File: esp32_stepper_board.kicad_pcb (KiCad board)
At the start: 2 copper layers, 99.9 x 70.2 mm, 30 parts, among them J1 Aux2_GPIO, J10 Aux1_I2C, J11 IO0_IO2_JP, J2 DC_PWR, J3 Servo, J4 Stepper A/X, J5 Stepper B/Y, J6 Stepper C/Y, J7 Endstop A/X, J8 Endstop B/Y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

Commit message: fix silk screen label for c/z stepper
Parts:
- J6: value Stepper C/Y -> Stepper C/Z
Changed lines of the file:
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@@
     (links 122)
     (no_connects 0)
-    (area 40.818999 32.436999 140.918001 102.818001)
+    (area 100.762999 63.271138 200.862001 135.530001)
     (thickness 1.6)
     (drawings 6)
@@
       (effects (font (size 1 1) (thickness 0.15)))
     )
-    (fp_text value "Stepper C/Y" (at 2.921 -3.048 180) (layer F.SilkS)
-      (effects (font (size 1 1) (thickness 0.15)))
-    )
+    (fp_text value "Stepper C/Z" (at 2.921 -3.048 180) (layer F.SilkS)
+      (effects (font (size 1 1) (thickness 0.15)))
+    )

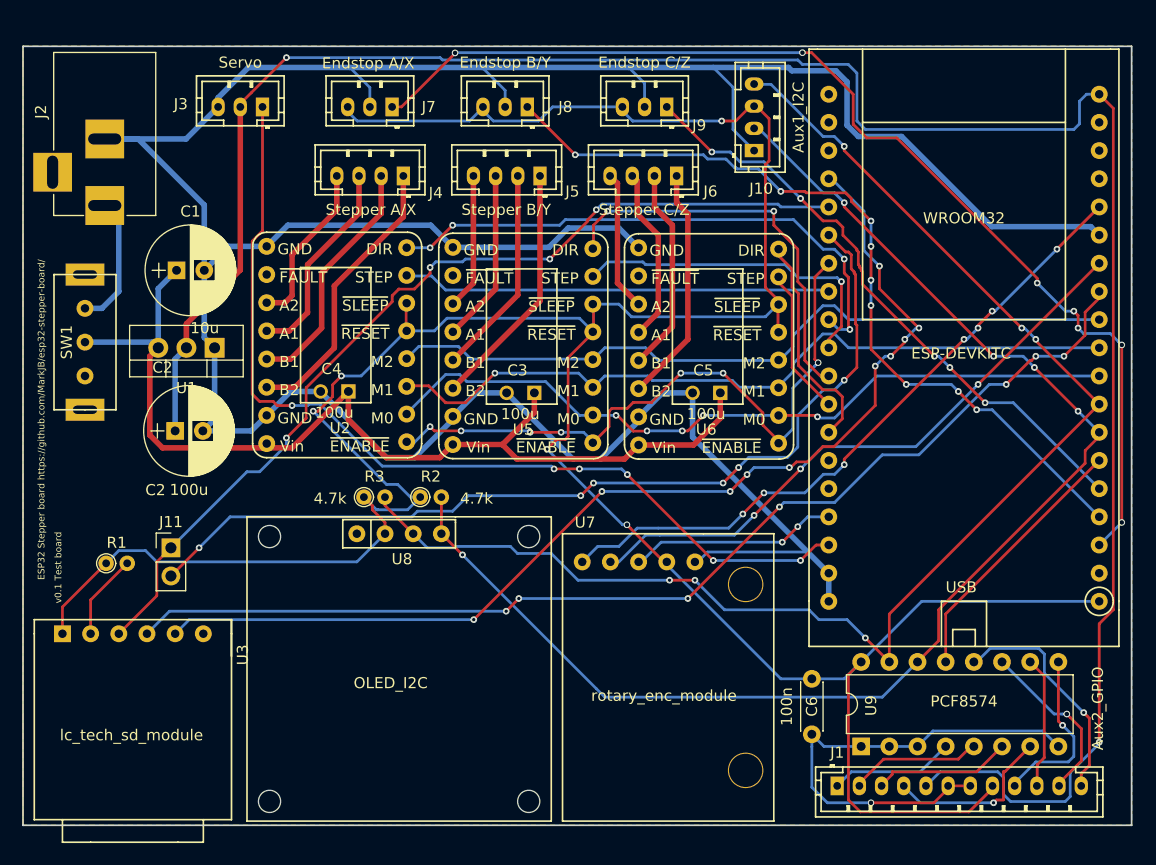
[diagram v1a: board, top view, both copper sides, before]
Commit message: Fixed devkit footprint and rerouted board
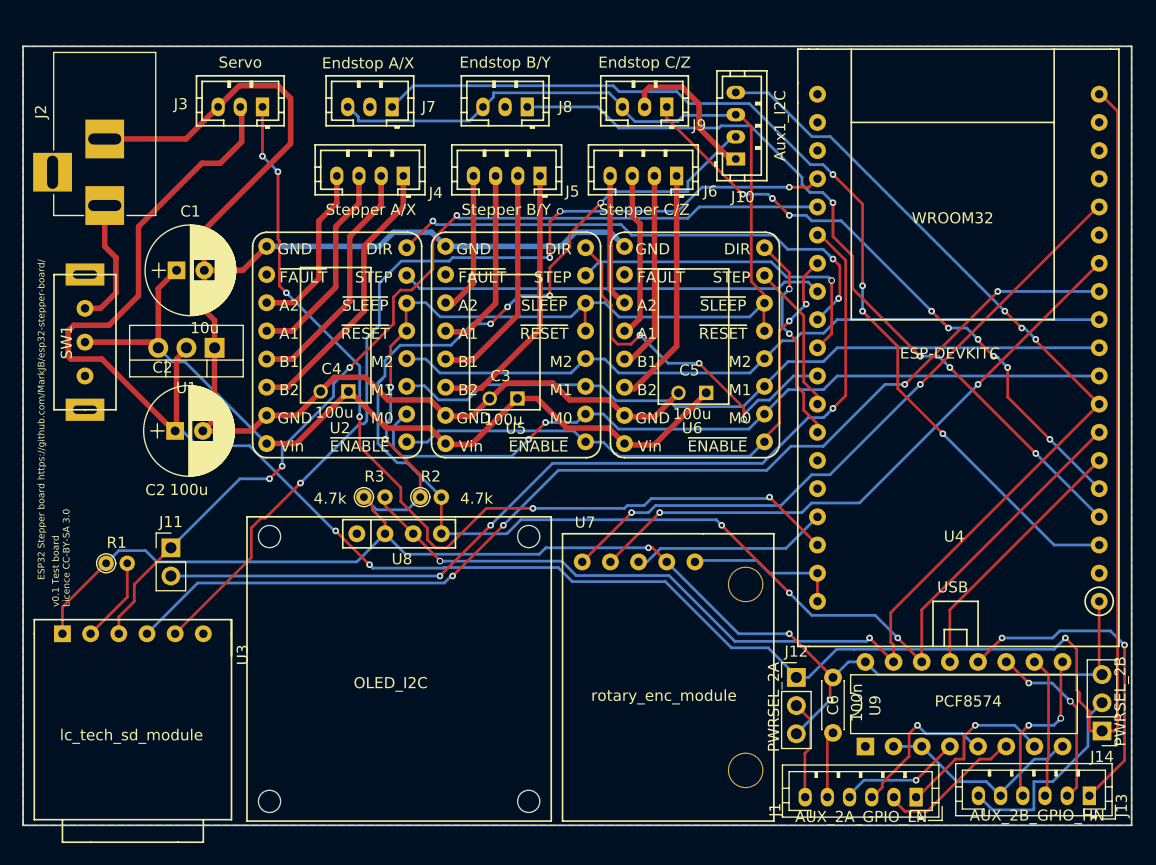
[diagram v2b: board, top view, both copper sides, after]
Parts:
- added J12: PWRSEL_2A, Pin_Headers:Pin_Header_Straight_1x03_Pitch2.54mm, F.Cu at (170.6, 120.4)
- added J13: AUX_2B_GPIO_HN, Connectors_JST:JST_PH_B6B-PH-K_06x2.00mm_Straight, F.Cu at (197.0, 131.1)
- added J14: PWRSEL_2B, Pin_Headers:Pin_Header_Straight_1x03_Pitch2.54mm, F.Cu at (198.1, 125.2)
- J1: value Aux2_GPIO -> AUX_2A_GPIO_LN; footprint Connectors_JST:JST_PH_B12B-PH-K_12x2.00mm_Straight -> Connectors_JST:JST_PH_B6B-PH-K_06x2.00mm_Straight
- moved J1 7.18 mm to (181.4, 131.2), turned to 180 degrees
- moved C6 1.91 mm to (173.9, 120.4)
- moved J10 1.82 mm to (165.1, 73.7)
- moved C3 1.61 mm to (145.4, 95.2)
- moved U6 1.28 mm to (161.9, 89.2)
- moved C5 1.27 mm to (162.4, 94.7)
- moved U5 0.66 mm to (145.8, 89.2)
- moved U9 0.38 mm to (176.8, 126.6)
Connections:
- J1 pad 1: /GPIO_EX0 -> /GPIO_EX3
- J1 pad 2: /GPIO_EX1 -> /GPIO_EX2
- J1 pad 3: /GPIO_EX2 -> /GPIO_EX1
- J1 pad 4: /GPIO_EX3 -> /GPIO_EX0
- J1 pad 5: /5v -> /GND
- J1 pad 6: /GND -> /PWR1
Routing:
- net /GND: track 336.7 -> 197.0 mm, vias 1 -> 0
- net /3v3: track 275.2 -> 246.7 mm
- net /PWR2: track 0.00 -> 18.7 mm
- net /SDA1: track 123.9 -> 138.5 mm, vias 5 -> 7
- net /12v: track 91.3 -> 76.7 mm
- net /5v: track 200.4 -> 213.5 mm, vias 2 -> 3
- net /SD_MISO: track 97.7 -> 85.0 mm, vias 10 -> 4
- net /~ES_A/X: track 100.1 -> 89.6 mm, vias 7 -> 4
- net /PWR1: track 0.00 -> 9.02 mm
- net /GPIO_EX7: track 20.9 -> 29.8 mm, vias 1 -> 2
- net /~STEP_EN: track 60.2 -> 52.8 mm, vias 7 -> 2
- net /A/X_DIR: track 50.9 -> 47.5 mm, vias 4 -> 3
- net /STEP_M0: track 68.6 -> 71.8 mm, vias 5 -> 2
- net /~ES_B/Y: track 73.8 -> 70.9 mm, vias 9 -> 4
- net /GPIO_EX1: track 11.9 -> 14.5 mm, vias 0 -> 1
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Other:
- board text added: "v0.1 Test board Licence CC-BY-SA 3.0"
- board text removed: "v0.1 Test board"

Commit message: fix flat cap silk and various silk issue
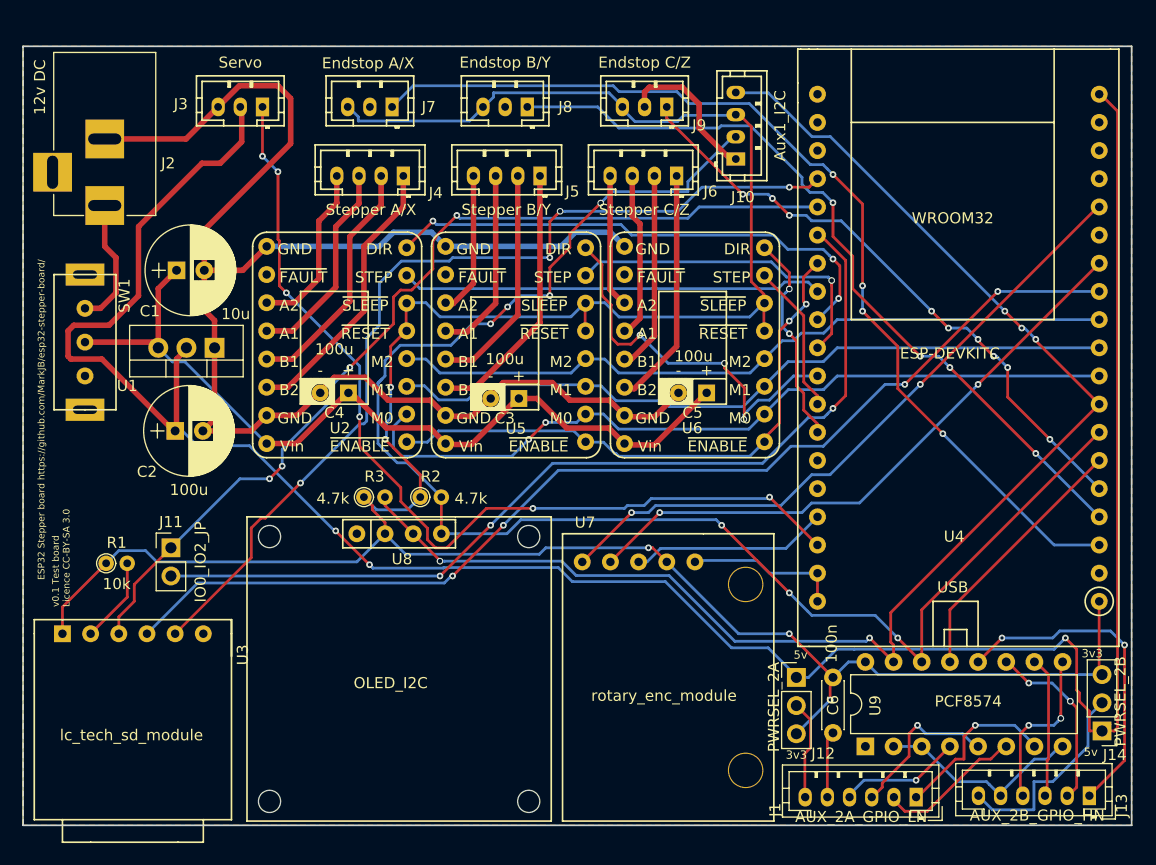
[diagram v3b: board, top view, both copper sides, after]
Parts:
- C3, C4, C5: footprint custom:C_Radial_lying_flat_D8_L11_P2.5 -> custom:Cap_laying_flat_2.5mm_lead_pitch
- moved C4 2.73 mm to (128.9, 97.0)
- moved C5 2.60 mm to (161.2, 97.0)
- moved C3 2.56 mm to (144.3, 97.5)
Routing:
- net /B/Y_DIR: track 33.9 -> 35.3 mm
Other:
- board text added: "12v DC"
- board text added: "3v3"
- board text added: "5v"

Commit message: Fixed devkitc footprint silk, rotated devkitc footprint, fix stepper pwr track width, c_step pin on IO23 (moved from gnd), moved renc_sw from tx.
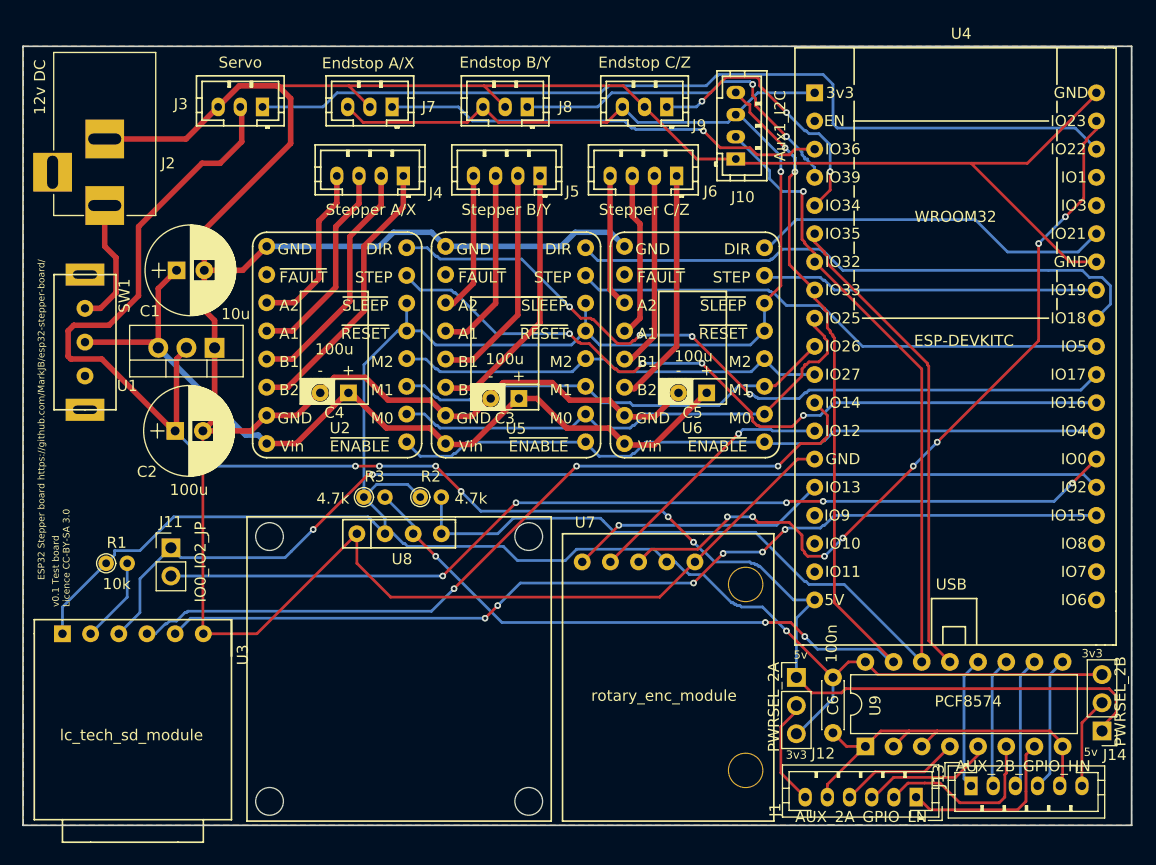
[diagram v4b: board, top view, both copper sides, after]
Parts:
- moved U4 52.5 mm to (172.2, 67.7), turned to 0 degrees
- moved J13 10.7 mm to (186.3, 130.2), turned to 0 degrees
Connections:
- U4 pad 32: /C/Z_DIR -> /GND
- U4 pad 33: /RX -> /C/Z_DIR
- U4 pad 34: /TX -> /RX
- U4 pad 35: /~RENC_SW -> /TX
- U4 pad 37: /GND -> /~RENC_SW
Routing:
- net /GND: track 197.2 -> 367.0 mm
- net /5v: track 213.5 -> 158.0 mm, vias 3 -> 6
- net /~RENC_SW: track 17.8 -> 70.3 mm, vias 0 -> 8
- net /~ES_A/X: track 89.6 -> 40.1 mm, vias 4 -> 1
- net /~ES_B/Y: track 70.9 -> 32.2 mm, vias 4 -> 2
- net /RENC_CLK: track 59.9 -> 23.7 mm, vias 2 -> 1
- net /RENC_DT: track 55.2 -> 23.4 mm, vias 2 -> 1
- net /A/X_STEP: track 38.1 -> 69.8 mm, vias 0 -> 4
- net /~ES_C/Z: track 55.5 -> 24.7 mm, vias 9 -> 3
- net /SDA1: track 138.5 -> 108.1 mm, vias 7 -> 1
- net /STEP_M2: track 66.3 -> 39.8 mm
- net /SD_SCK: track 98.6 -> 72.3 mm, vias 4 -> 3
- net /STEP_M1: track 66.8 -> 41.4 mm
- net /STEP_M0: track 71.8 -> 46.8 mm, vias 2 -> 0
- net /A/X_DIR: track 47.5 -> 69.5 mm, vias 3 -> 4
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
